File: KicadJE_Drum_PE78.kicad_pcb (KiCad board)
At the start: 2 copper layers, 183 x 128 mm, 189 parts, among them J101 Snare, J102 LCymbals, J103 SCymbals, J104 Maracas, J105 Bass, J106 LBongo, J107 HBongo, J108 Claves, J201 AudioJack2_SwitchT, J202 AudioJack2_SwitchT, J203 AudioJack2_SwitchT, J204 Power +, J205 Power -, J206 Conn_01x03_Male, J207 Conn_01x03_Male, J208 Conn_01x03_Male, J209 Conn_01x03_Male, J210 Conn_01x02_Male, J301 Tone/Noise, J302 RND, J303 Noise, J304 DRUM_OUT, J305 Tones, J306 Noise, P101 HEADER_2x8_Doepfer, P201 HEADER_2x5_Doepfer, Q101 2N3904, Q102 2N3904, Q103 2N3904, Q104 2N3904, SW201 SW_SPDT, U101 74HC04, U302 TL072

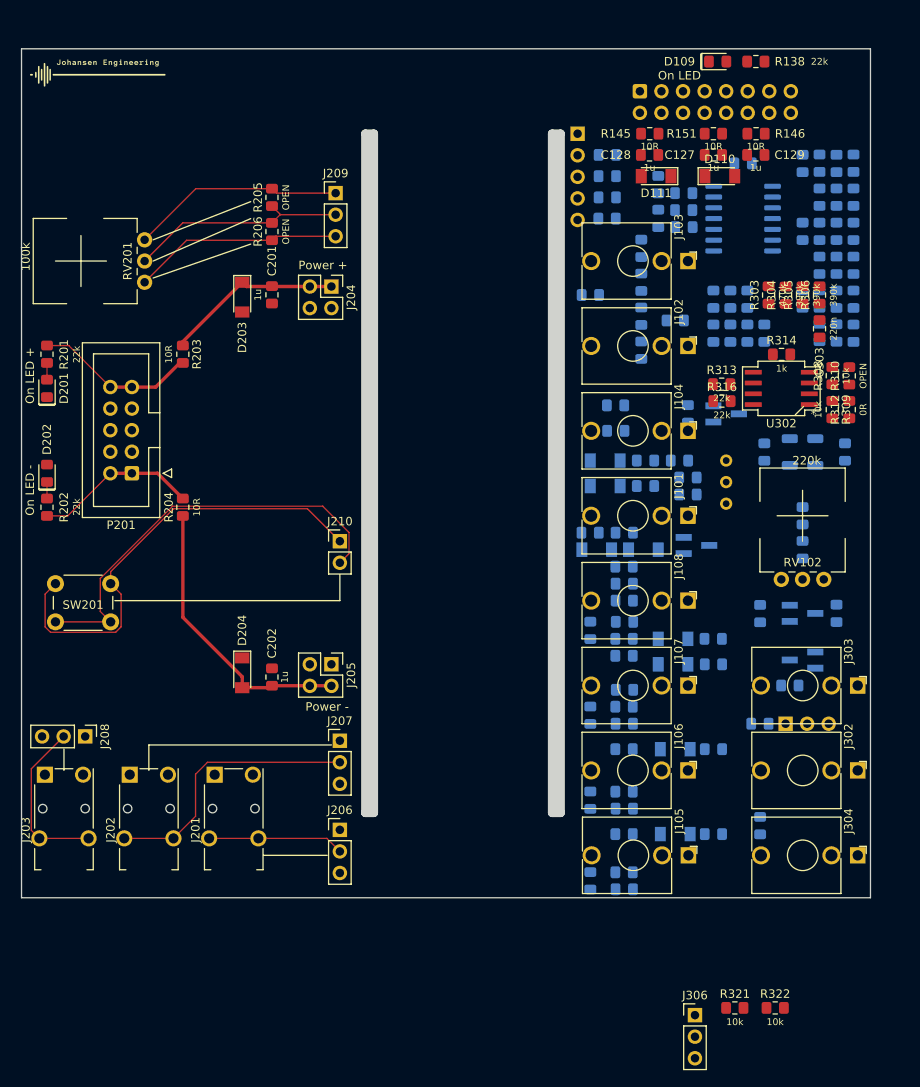
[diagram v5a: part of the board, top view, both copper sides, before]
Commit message: BB Logo - GND planes
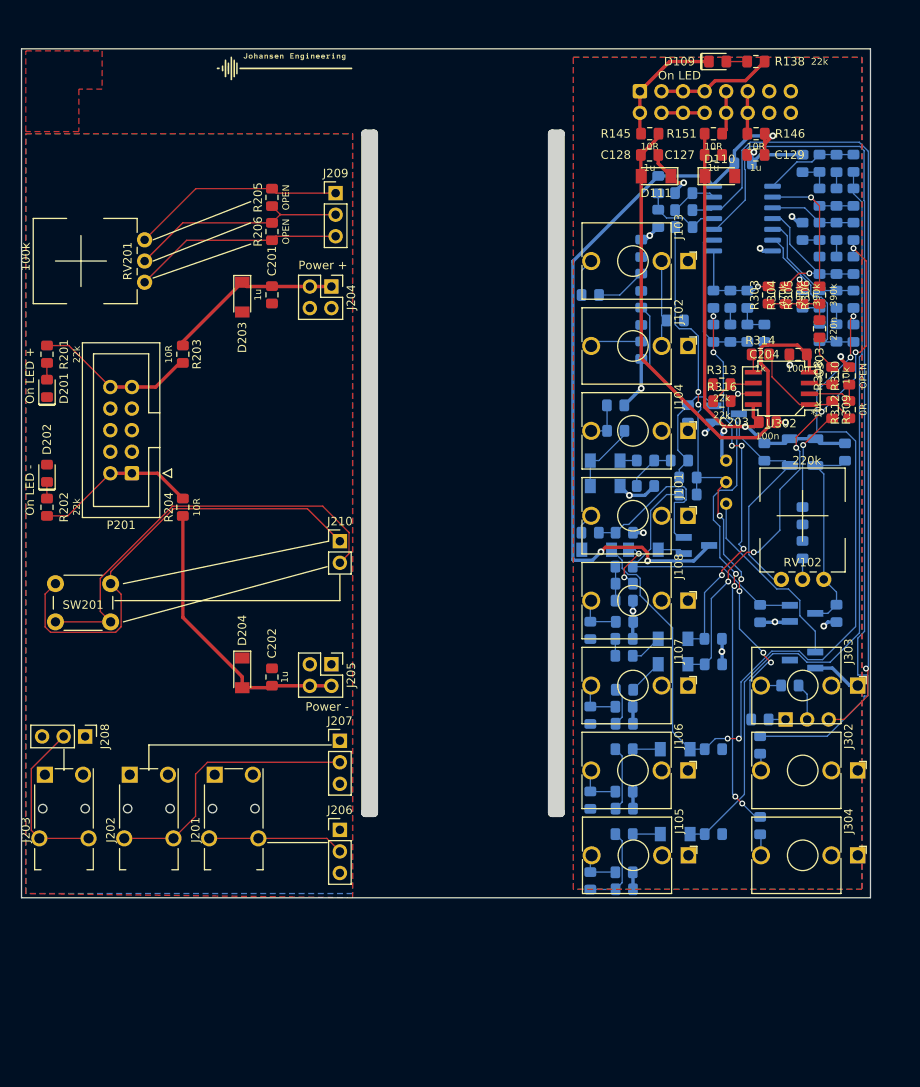
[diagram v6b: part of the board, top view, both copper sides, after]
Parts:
- removed J305: Tones, Connector_PinHeader_2.54mm:PinHeader_1x05_P2.54mm_Vertical
- removed J306: Noise, Connector_PinHeader_2.54mm:PinHeader_1x03_P2.54mm_Vertical
- removed R317: 470k, AJ:R_0805_AJ
- removed R318, R319, R320: 390k, AJ:R_0805_AJ
- removed R321, R322: 10k, AJ:R_0805_AJ
- added C203: 100n, AJ:C_0805_AJ, F.Cu at (137.9, 94.0)
- added C204: 100n, AJ:C_0805_AJ, F.Cu at (141.5, 86.0)
- added G***: LOGO, AJ:Johansen_engineering_soldermask_20mm, F.Cu at (58.5, 52.2)
- added R323: 470R, AJ:R_0805_AJ, B.Cu at (137.0, 132.0)
- moved G*** 22.0 mm to (81.0, 52.2)
- moved R314 2.50 mm to (137.0, 86.0)
- moved J301 0.50 mm to (140.0, 129.0)
- moved R311 0.50 mm to (137.0, 129.0)
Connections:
- J102 pad TN: Net-(J101-PadTN) -> Net-(J102-PadTN)
- J103 pad TN: Net-(J101-PadTN) -> Net-(J102-PadTN)
- R101 pad 2: Net-(J101-PadTN) -> Net-(J102-PadTN)
- U101 pad 10: Net-(J302-PadT) -> Net-(R323-Pad2)
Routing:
- net Net-(R323-Pad2): track 0.00 -> 106.0 mm
- net LBongoTrig: track 0.00 -> 102.2 mm, vias 0 -> 4
- net Net-(J301-Pad3): track 0.00 -> 97.2 mm, vias 0 -> 1
- net BassTrig: track 0.00 -> 93.2 mm
- net +5V: track 0.00 -> 90.6 mm, vias 0 -> 3
- net GND: track 0.00 -> 82.8 mm, vias 0 -> 16
- net NoiseOut: track 0.00 -> 69.8 mm, vias 0 -> 7
- net -12Vc: track 33.7 -> 98.3 mm
- net HBongoTrig: track 0.00 -> 62.8 mm, vias 0 -> 6
- net Net-(R315-Pad2): track 0.00 -> 60.2 mm, vias 0 -> 5
- net +12Vc: track 21.1 -> 81.0 mm, vias 0 -> 2
- net ClavesTrig: track 0.00 -> 46.2 mm, vias 0 -> 6
- net Net-(C111-Pad2): track 0.00 -> 32.0 mm
- net Net-(C112-Pad1): track 0.00 -> 29.5 mm
- net Net-(L104-Pad2): track 0.00 -> 27.5 mm
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- added copper zone on F.Cu, net (none)

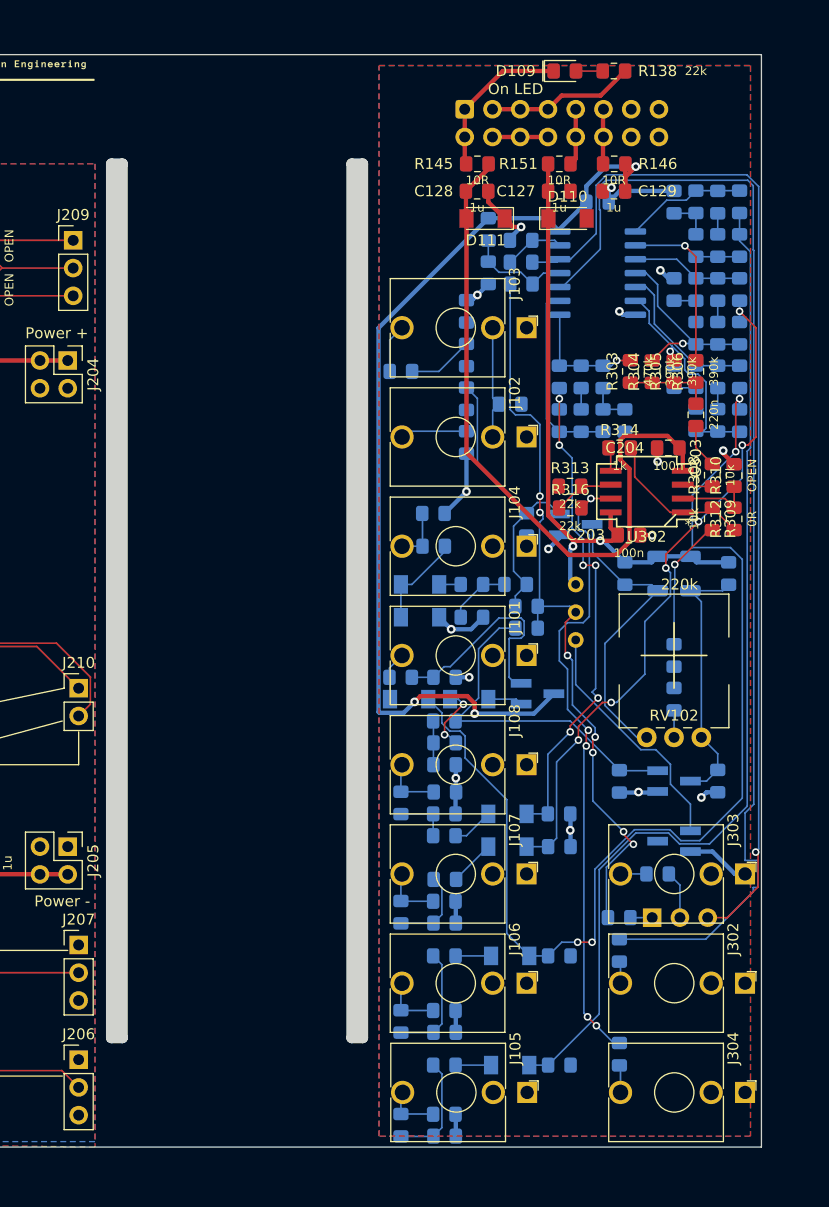
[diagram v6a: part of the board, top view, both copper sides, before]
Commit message: Front Component Silk
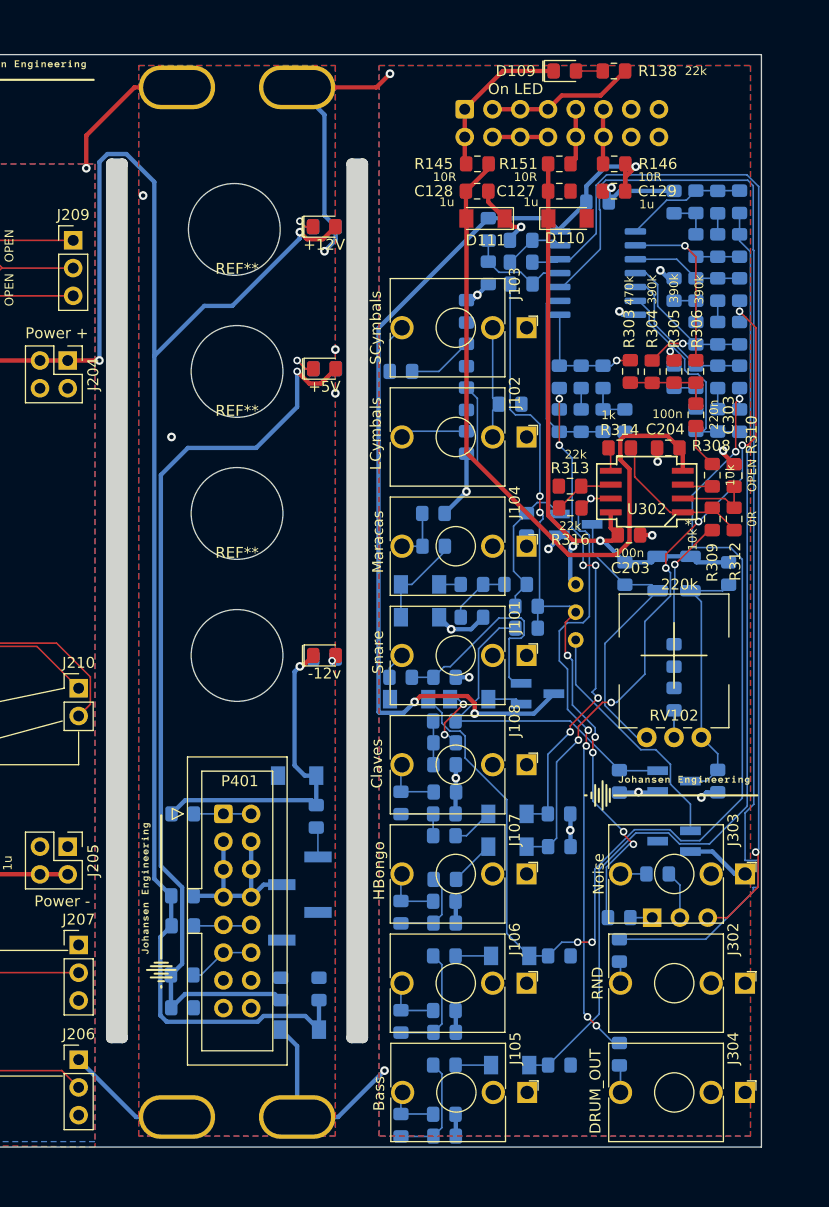
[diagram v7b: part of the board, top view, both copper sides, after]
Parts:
- added C401: 1u, AJ:C_0805_AJ, B.Cu at (97.0, 127.0)
- added C403: 1u, AJ:C_0805_AJ, B.Cu at (97.0, 137.2)
- added D401: +12V, AJ:D_0805_AJ, F.Cu at (110.0, 65.8)
- added D402: +5V, AJ:D_0805_AJ, F.Cu at (110.0, 78.8)
- added D403: -12v, AJ:D_0805_AJ, F.Cu at (110.0, 105.0)
- added D404: 1N4007, Diode_SMD:D_MiniMELF, B.Cu at (107.8, 139.2)
- added D405: 1N4007, Diode_SMD:D_MiniMELF, B.Cu at (107.5, 116.0)
- added G***: LOGO, AJ:Johansen_engineering_logo_20mm, F.Cu at (95.0, 127.5)
- added G***: LOGO, AJ:Johansen_engineering_logo_20mm, F.Cu at (141.8, 117.8)
- added H103: MountingHole_Pad, AJ:MountingHole_Eurorack3, B.Cu at (107.5, 53.0)
- added H103: MountingHole_Pad, AJ:MountingHole_Eurorack3, B.Cu at (96.5, 53.0)
- added H103: MountingHole_Pad, AJ:MountingHole_Eurorack3, B.Cu at (107.5, 147.2)
- added H103: MountingHole_Pad, AJ:MountingHole_Eurorack3, B.Cu at (96.5, 147.2)
- added J401: Tone/Noise, Connector_PinHeader_2.54mm:PinHeader_1x04_P2.54mm_Vertical_SMD_Pin1Left, B.Cu at (107.8, 127.2)
- added P401: HEADER_2x8_Doepfer, Connector_IDC:IDC-Header_2x08_P2.54mm_Vertical, F.Cu at (100.8, 119.5)
- added R401: 0R, AJ:R_0805_AJ, B.Cu at (97.0, 134.2)
- added R402: 0R, AJ:R_0805_AJ, B.Cu at (97.0, 129.8)
- added R403: 0R, AJ:R_0805_AJ, B.Cu at (97.0, 119.5)
- added R404: 22k, AJ:R_0805_AJ, B.Cu at (110.0, 65.8)
- added R405: 10k, AJ:R_0805_AJ, B.Cu at (110.0, 78.8)
- added R406: 22k, AJ:R_0805_AJ, B.Cu at (110.0, 105.2)
- added R407: 10R, AJ:R_0805_AJ, B.Cu at (106.0, 135.5)
- added R408: 10R, AJ:R_0805_AJ, B.Cu at (109.5, 135.5)
- added R409: 10R, AJ:R_0805_AJ, B.Cu at (109.2, 119.7)
- added REF**: MountingHole_8.4mm_M8, MountingHole:MountingHole_8.4mm_M8, F.Cu at (101.8, 66.0)
- added REF**: MountingHole_8.4mm_M8, MountingHole:MountingHole_8.4mm_M8, F.Cu at (102.0, 79.0)
- added REF**: MountingHole_8.4mm_M8, MountingHole:MountingHole_8.4mm_M8, F.Cu at (102.0, 92.0)
- added REF**: MountingHole_8.4mm_M8, MountingHole:MountingHole_8.4mm_M8, F.Cu at (102.0, 105.0)
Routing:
- net +12Vc: track 81.0 -> 226.4 mm, vias 2 -> 4
- net GND: track 82.8 -> 170.1 mm, vias 16 -> 22
- net +5V: track 90.6 -> 174.3 mm, vias 3 -> 4
- net -12Vc: track 98.3 -> 128.2 mm, vias 0 -> 1
- net /KicadJE_PDU_1/+5: track 0.00 -> 6.14 mm
- net /KicadJE_PDU_1/+12: track 0.00 -> 5.28 mm
- net /KicadJE_PDU_1/-12: track 0.00 -> 5.24 mm
- net Net-(D402-Pad1): track 0.00 -> 3.60 mm, vias 0 -> 1
- net Net-(D401-Pad1): track 0.00 -> 2.84 mm, vias 0 -> 1
- net Net-(J401-Pad4): track 0.00 -> 2.75 mm
- net Net-(D403-Pad2): track 0.00 -> 1.04 mm, vias 0 -> 1
- net (no net): vias 0 -> 2
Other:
- board text added: "KicadJE-PDU1 27/4/2021 Rev A"
- board text added: "PDU1"
